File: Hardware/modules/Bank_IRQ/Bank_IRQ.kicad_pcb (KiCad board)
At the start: 4 copper layers, 83.3 x 68.2 mm, 33 parts, among them J2 Bus_PCI_6502, U1 74HC00, U2 74HC138, U3 6525

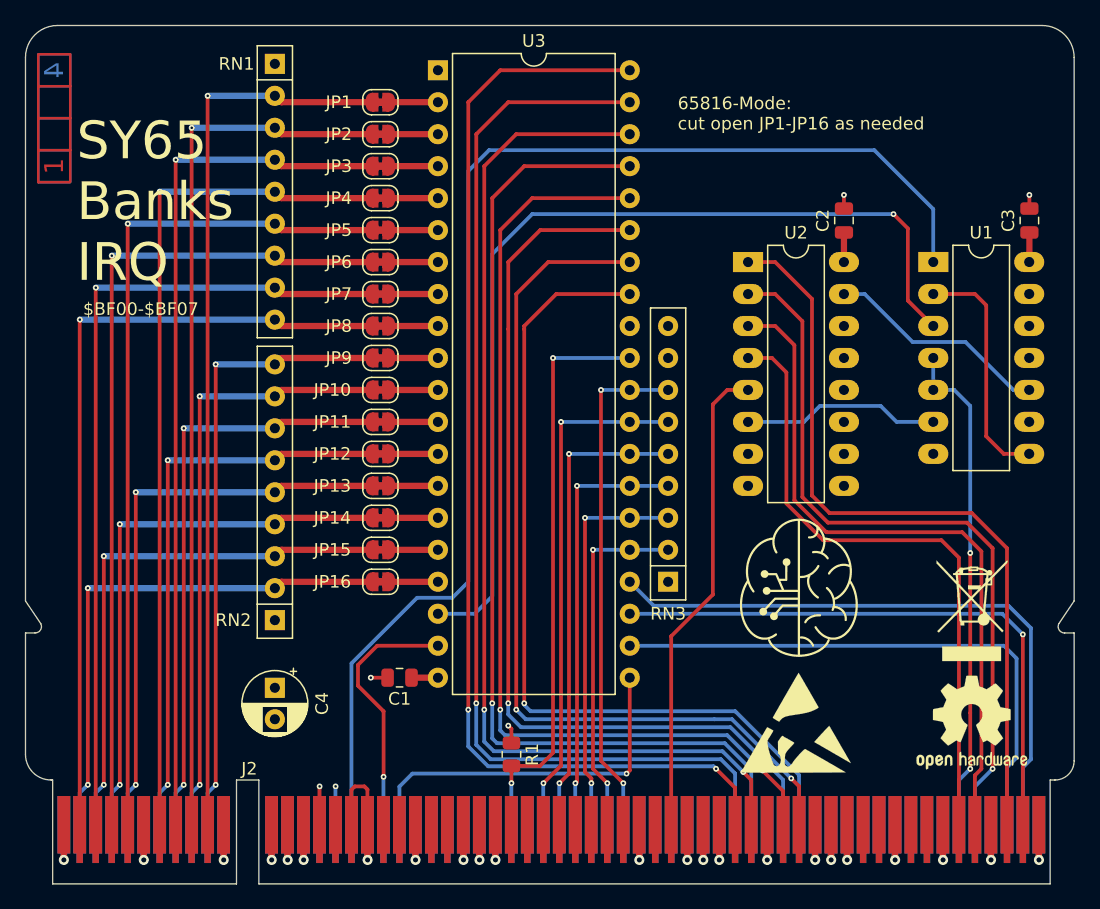
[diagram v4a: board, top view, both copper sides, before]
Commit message: Big Review Update - Changed Copper Pours on all PCBs - Implemented errors found at review - fixed some additional errors
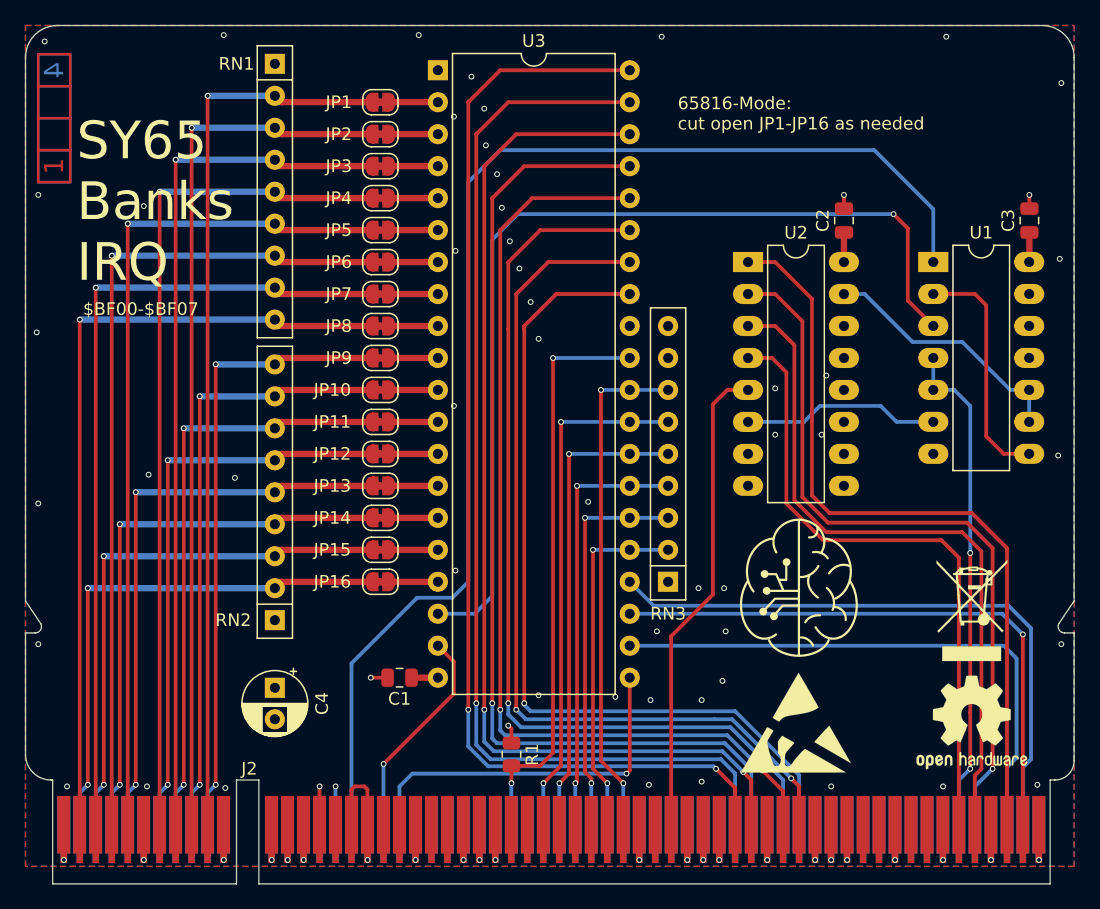
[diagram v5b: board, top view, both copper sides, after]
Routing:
- net /R/~{W}: track 20.5 -> 17.1 mm
- net Net-(U2-~{Y0}): track 17.9 -> 20.4 mm
- net Net-(U3-~{CS}): track 75.5 -> 76.1 mm
- net /CLK: track 101.2 -> 100.7 mm
- net +5V: vias 4 -> 56
- added copper zone on B.Cu, net +5V
- added copper zone on F.Cu, net +5V
- added copper zone on In1.Cu, net GND
- removed copper zone on In1.Cu, net +5V
